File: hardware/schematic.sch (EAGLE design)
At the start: 28 parts, among them J1 SMA_EDGE, U1 HX1

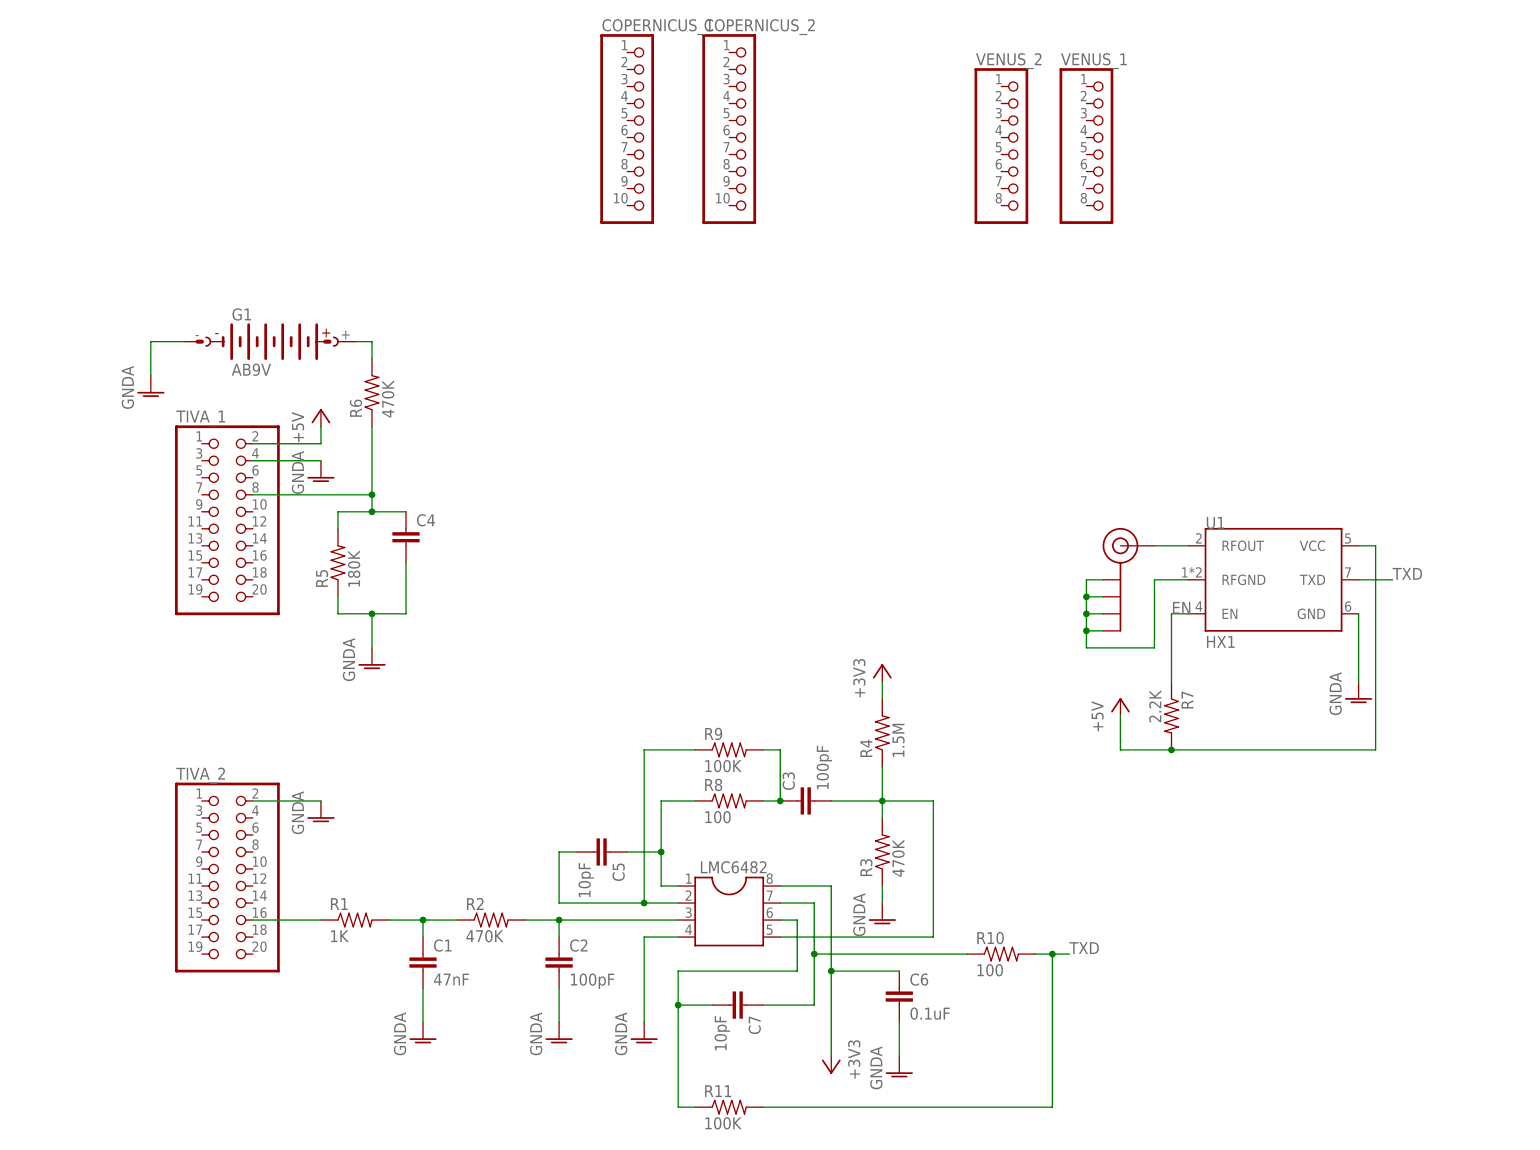
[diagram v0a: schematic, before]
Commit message: Update PCB to include VRM module, change all components to 0805, and upgrade silkscreen
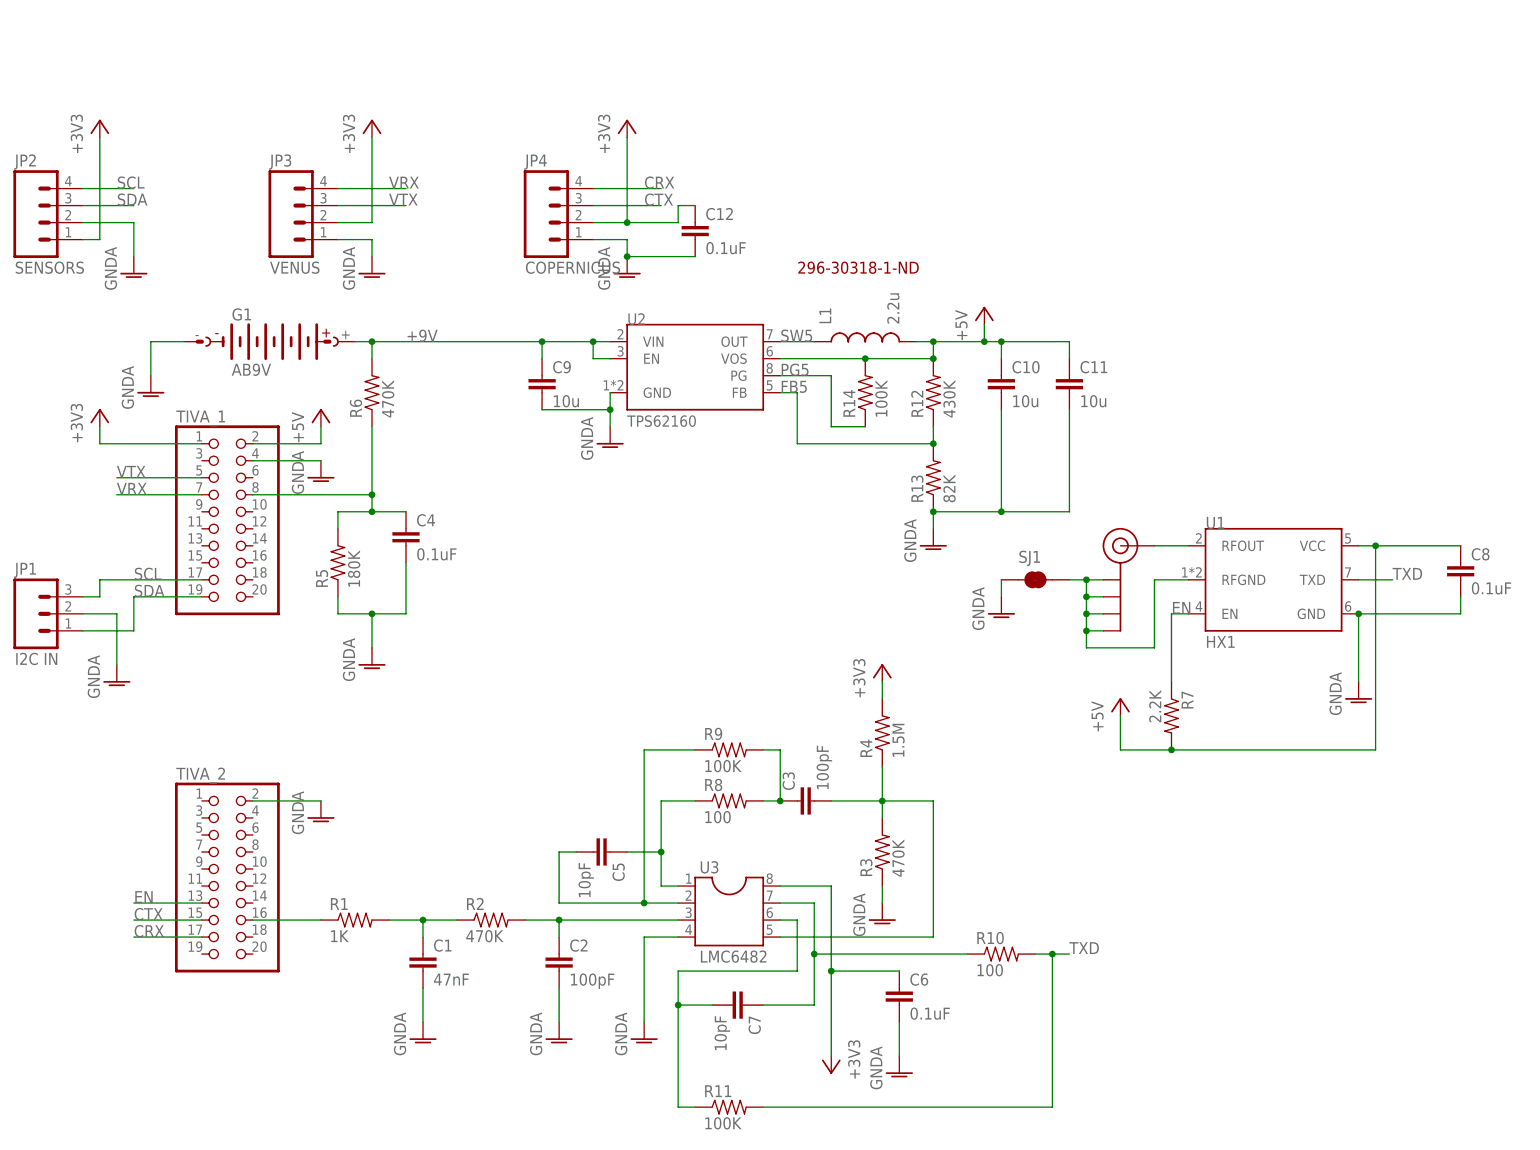
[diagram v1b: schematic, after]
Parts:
- removed COPERNICUS_1, COPERNICUS_2: (no value), pinhead:PINHD-1X10
- removed VENUS_1, VENUS_2: (no value), pinhead:PINHD-1X8
- added C10, C11, C9: 10u, SparkFun-Passives:CAP0805
- added C12, C8: 0.1uF, SparkFun-Passives:CAP0805
- added JP1: I2C IN, SparkFun-Connectors:M03PTH
- added JP2: SENSORS, SparkFun-Connectors:M04PTH
- added JP3: VENUS, SparkFun-Connectors:M04PTH
- added JP4: COPERNICUS, SparkFun-Connectors:M04PTH
- added L1: 2.2u, HAB:INDUCTOR
- added R12: 430K, SparkFun-Passives:RESISTOR0805-RES
- added R13: 82K, SparkFun-Passives:RESISTOR0805-RES
- added R14: 100K, SparkFun-Passives:RESISTOR0805-RES
- added SJ1: JUMPER-PAD-2-NC_BY_TRACE, SparkFun-Passives:JUMPER-PAD-2-NC_BY_TRACE
- added U2: TPS62160, HAB:TPS62160
- C1, C2, C3, C5, C6, C7: device SparkFun-Passives:CAP1206 -> SparkFun-Passives:CAP0805
- C4: value (none) -> 0.1uF; device SparkFun-Passives:CAP1206 -> SparkFun-Passives:CAP0805
- R1, R10, R11, R2, R3, R4, R5, R6, R7, R8, R9: device SparkFun-Passives:RESISTOR1206 -> SparkFun-Passives:RESISTOR0805-RES
- U3: value (none) -> LMC6482
- renumbered LMC6482 to U3
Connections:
- new net CRX: JP4.4, TIVA_2.17
- new net CTX: JP4.3, TIVA_2.15
- new net FB5: R12.1, R13.2, U2.FB
- new net PG5: R14.1, U2.PG
- new net SCL: JP1.3, JP2.4, TIVA_1.17
- new net SDA: JP1.1, JP2.3, TIVA_1.19
- new net SW5: L1.1, U2.OUT
- new net VRX: JP3.4, TIVA_1.7
- new net VTX: JP3.3, TIVA_1.5
- net +3V3: now also C12.1, JP2.1, JP3.2, JP4.2, TIVA_1.1
- net +5V: now also C10.1, C11.1, C8.1, L1.2, R12.2, R14.2, U2.VOS
- net +9V: now also C9.1, U2.EN, U2.VIN
- net EN: now also TIVA_2.13
- net GNDA: now also C10.2, C11.2, C12.2, C8.2, C9.2, JP1.2, JP2.2, JP3.1, JP4.1, R13.1, SJ1.1, U2.GND
- net RFGND: now also SJ1.2
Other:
- note added: "296-30318-1-ND"
